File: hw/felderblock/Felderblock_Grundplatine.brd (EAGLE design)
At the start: 100 x 78 mm, 50 parts, among them IC1 LM311N, IC2 LM2936, J1 RJ11, J2 RJ11, M1 ARDUINO-NANO-3.0, T2 BC337, X1 TASTENSPERRE1, X2 TASTENSPERRE2, X3 SCHL-SPERRE, X5 ANSCHALTER

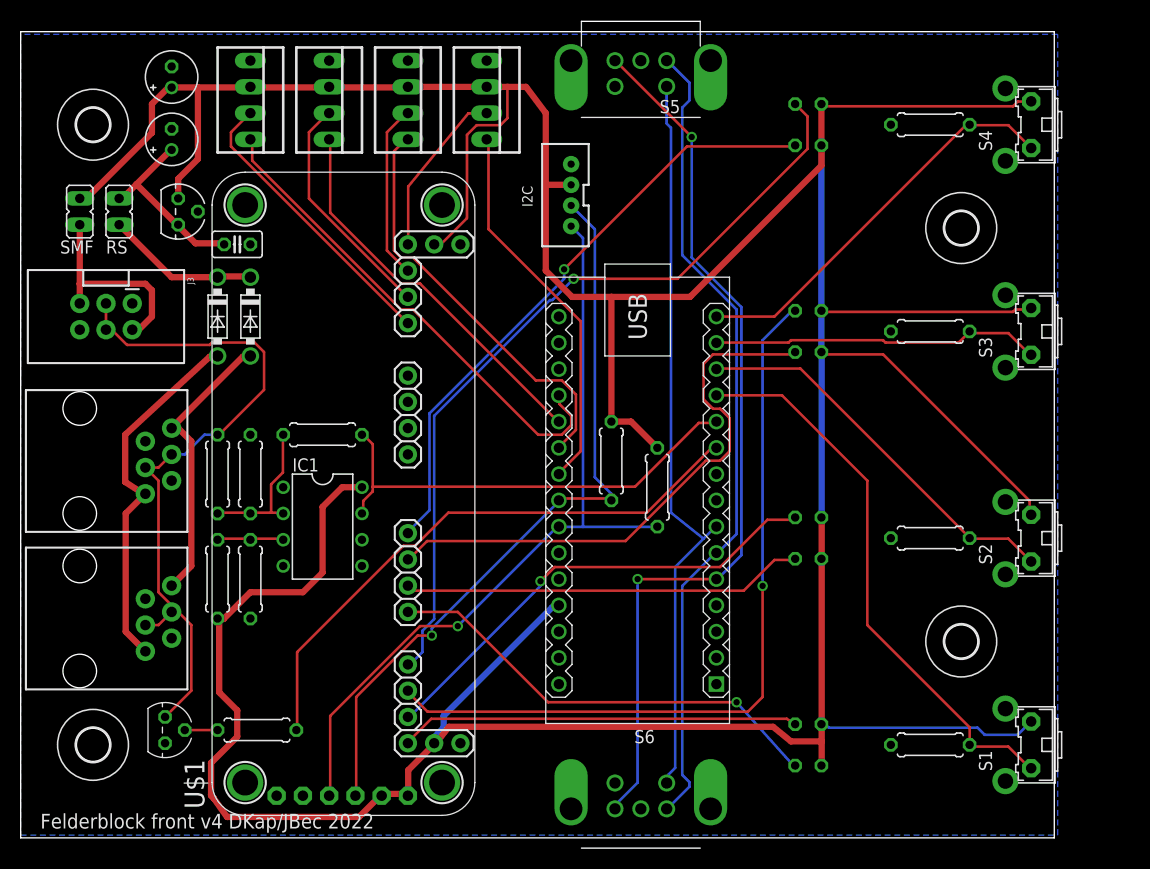
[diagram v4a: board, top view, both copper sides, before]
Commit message: Changed footprint for voltage regulator to TO220
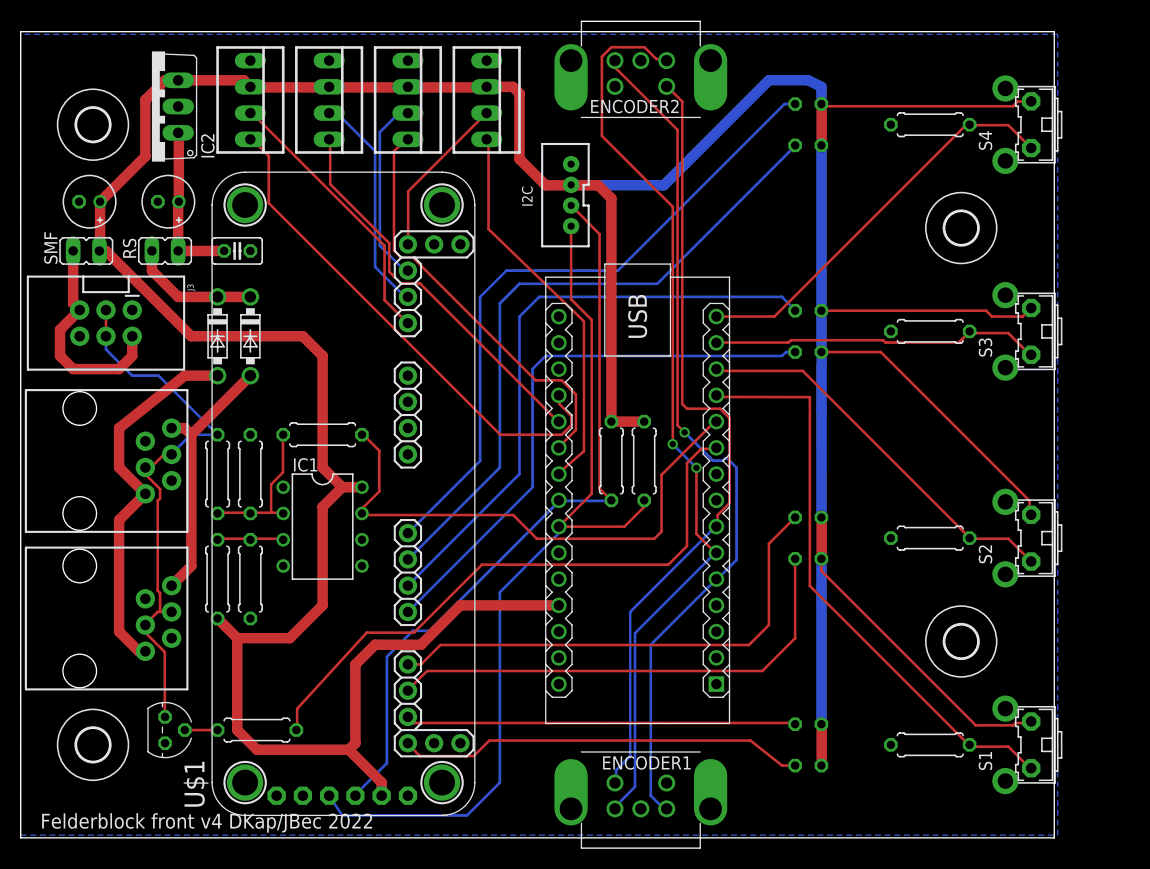
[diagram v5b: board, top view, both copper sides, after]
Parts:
- ENCODER1, ENCODER2: value EC11B42AE -> (none)
- IC2: value LM2936 -> MC78M05CT; device national-semiconductor:TO92 -> linear:TO220V
- LED1, LED2, LED3, LED4: value (none) -> Red
- LED5, LED6, LED7, LED8: value (none) -> White
- R3: value 4.7k -> 4k7
- moved C5 14.4 mm to (6.67, 62.5), turned to 180 degrees
- moved IC2 10.5 mm to (12.7, 71.8), turned to 90 degrees
- moved C4 6.04 mm to (14.3, 62.5), turned to 180 degrees
- moved RS 5.85 mm to (14.0, 57.8), turned to 90 degrees
- moved LED1 4.00 mm to (76.2, 8.00)
- moved LED2 4.00 mm to (76.2, 28.0)
- moved LED3 4.00 mm to (76.2, 48.0)
- moved LED4 4.00 mm to (76.2, 68.0)
- moved LED5 4.00 mm to (76.2, 12.0)
- moved LED6 4.00 mm to (76.2, 32.0)
- moved LED7 4.00 mm to (76.2, 52.0)
- moved LED8 4.00 mm to (76.2, 72.0)
- moved SMF 3.86 mm to (6.35, 57.8), turned to 90 degrees
- moved R1 2.84 mm to (60.3, 37.5)
- moved D1 1.91 mm to (22.2, 49.5)
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- renumbered S5 to ENCODER2, S6 to ENCODER1
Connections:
- net FELD4_LED_WS renamed FELD4_LED_WT
- removed net FELD1_LED_WS: LED5.K, U$1.33
- removed net FELD2_LED_WS: LED6.K, U$1.36
- removed net FELD3_LED_WS: LED7.K, U$1.39
- new net FELD1_LED_WT: LED5.K, U$1.6
- new net FELD2_LED_WT: LED6.K, U$1.12
- new net FELD3_LED_WT: LED7.K, U$1.36
- net +5V: now also IC2.3; no longer IC2.1, U$1.19, U$1.2, U$1.53
- net FELD2_LED_RD: now also U$1.9; no longer U$1.6
- net FELD3_LED_RD: now also U$1.33; no longer U$1.9
- net FELD4_LED_RD: now also U$1.39; no longer U$1.12
- net N$7: now also IC2.1; no longer IC2.3
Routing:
- net FELD3_LED_WT: track 0.00 -> 58.6 mm
- net FELD3_LED_WS: track 54.8 -> 0.00 mm
- net FELD2_LED_WT: track 0.00 -> 48.0 mm
- net FELD1_LED_WS: track 43.8 -> 0.00 mm, vias 1 -> 0
- net FELD2_LED_WS: track 38.9 -> 0.00 mm
- net FELD1_LED_WT: track 0.00 -> 37.8 mm
- net +5V: track 435.5 -> 410.7 mm
- net FELD3_LED_RD: track 74.6 -> 54.6 mm, vias 1 -> 0
- net FELD4_LED_RD: track 77.1 -> 63.4 mm, vias 1 -> 0
- net LOCONET: track 67.6 -> 53.9 mm
- net SCL: track 76.8 -> 87.0 mm, vias 1 -> 0
- net MI_REV: track 79.3 -> 88.9 mm, vias 0 -> 2
- net LN_RX: track 44.4 -> 52.6 mm
- net FELD4_LED_WT: track 59.1 -> 64.0 mm, vias 1 -> 0
- net MI_SW: track 72.3 -> 76.4 mm
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
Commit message: Extended to six fields
Extended to six fields per PCB
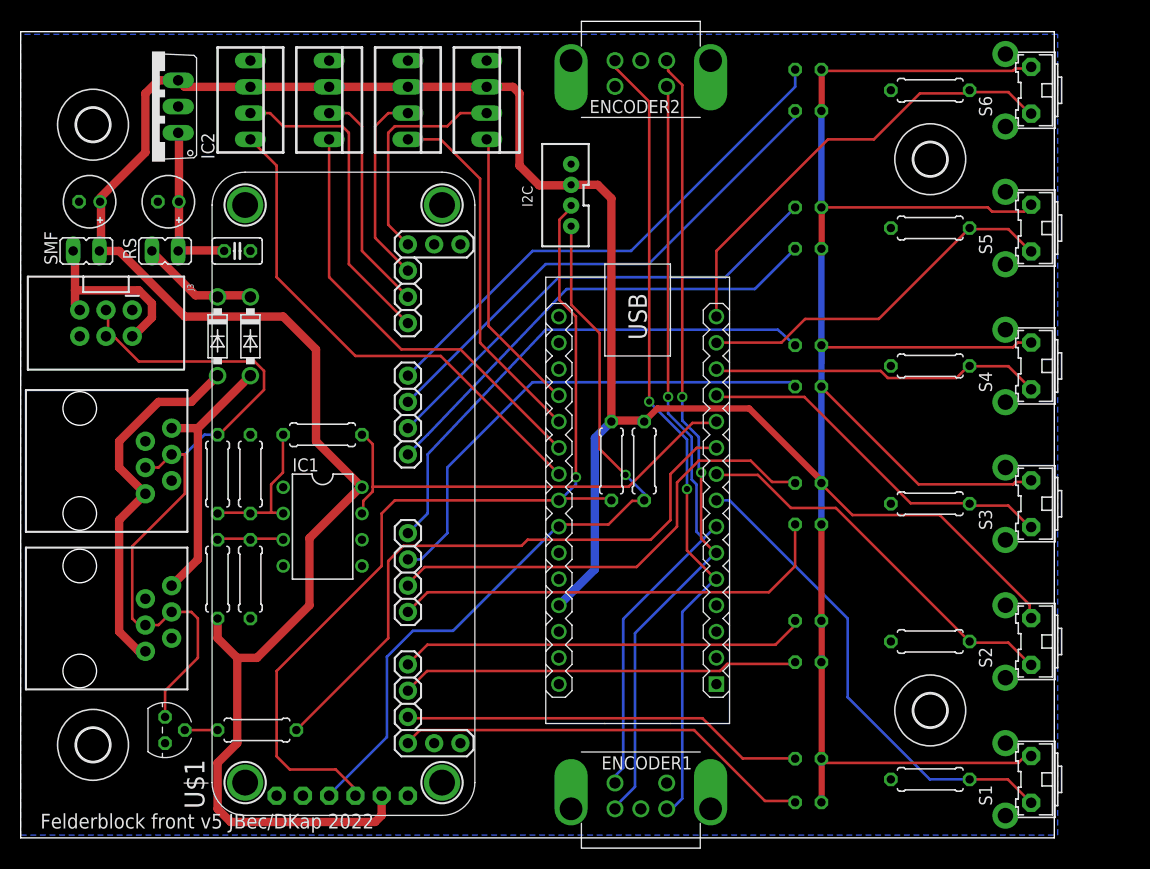
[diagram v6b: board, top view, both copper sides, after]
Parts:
- added LED10, LED11, LED12, LED9: White, led:LED3MM
- added R4, R5: 10k, resistor:0207/7
- added S5, S6: (no value), adafruit:B3F-31XX
- LED5, LED6: value White -> Red
- moved LED8 50.0 mm to (76.2, 22.0)
- moved LED5 46.0 mm to (76.2, 58.0)
- moved LED7 43.3 mm to (76.2, 8.66)
- moved LED6 39.3 mm to (76.2, 71.3)
- moved LED4 23.3 mm to (76.2, 44.7)
- moved R7 23.3 mm to (88.0, 46.7)
- moved S4 23.3 mm to (96.5, 46.7)
- moved LED3 16.7 mm to (76.2, 31.3)
- moved R8 16.7 mm to (88.0, 33.3)
- moved S3 16.7 mm to (96.5, 33.3)
- moved LED2 10.0 mm to (76.2, 18.0)
- moved R9 10.0 mm to (88.0, 20.0)
- moved S2 10.0 mm to (96.5, 20.0)
- moved H1 7.31 mm to (88.0, 13.3)
- moved H4 7.30 mm to (88.0, 66.7)
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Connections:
- new net FELD5_LED_RD: LED5.K, U$1.57
- new net FELD5_LED_WT: LED11.K, U$1.60
- new net FELD5_SW: M1.J1.14, R4.1, S5.1
- new net FELD6_LED_RD: LED6.K, U$1.63
- new net FELD6_LED_WT: LED12.K, U$1.66
- new net FELD6_SW: M1.J1.15, R5.1, S6.1
- net +5V: now also LED10.A, LED11.A, LED12.A, LED9.A, S5.2, S6.2
- net AS_SW: now also M1.J2.12; no longer M1.J2.9
- net FELD1_LED_WT: now also LED7.K; no longer LED5.K
- net FELD1_SW: now also M1.J1.8; no longer M1.J1.12
- net FELD2_LED_WT: now also LED8.K; no longer LED6.K
- net FELD2_SW: now also M1.J1.9; no longer M1.J1.13
- net FELD3_LED_WT: now also LED9.K; no longer LED7.K
- net FELD3_SW: now also M1.J1.12; no longer M1.J1.14
- net FELD4_LED_WT: now also LED10.K; no longer LED8.K
- net FELD4_SW: now also M1.J1.13; no longer M1.J1.15
- net GND: now also R4.2, R5.2
- net SCHL_SP_SW: now also M1.J2.11; no longer M1.J2.10
- net TSP1_SW: now also M1.J2.9; no longer M1.J2.12
- net TSP2_SW: now also M1.J2.10; no longer M1.J2.11
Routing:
- net FELD6_LED_WT: track 0.00 -> 50.7 mm
- net FELD6_LED_RD: track 0.00 -> 49.5 mm
- net FELD5_LED_WT: track 0.00 -> 46.3 mm
- net FELD5_LED_RD: track 0.00 -> 46.1 mm
- net FELD6_SW: track 0.00 -> 44.2 mm
- net FELD5_SW: track 0.00 -> 36.0 mm
- net +5V: track 410.7 -> 443.6 mm, vias 0 -> 1
- net LOCONET: track 53.9 -> 73.4 mm
- net SDA: track 72.9 -> 90.9 mm, vias 0 -> 1
- net FELD4_LED_RD: track 63.4 -> 48.5 mm
- net FELD4_LED_WT: track 64.0 -> 49.7 mm
- net FELD3_LED_WT: track 58.6 -> 45.9 mm
- net FELD3_LED_RD: track 54.6 -> 43.3 mm
- net SCL: track 87.0 -> 76.4 mm, vias 0 -> 1
- net MI_REV: track 88.9 -> 78.7 mm
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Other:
- board text added: "Felderblock front v5 JBec/DKap 2022"
- board text removed: "Felderblock front v4 DKap/JBec 2022"
